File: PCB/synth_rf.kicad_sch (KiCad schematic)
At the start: 63 parts, among them J2 SMA CLK0, J3 SMA CLK1, J4 SMA CLK2, U2 Si5351A-B-GT, X1 25MHz TCXO

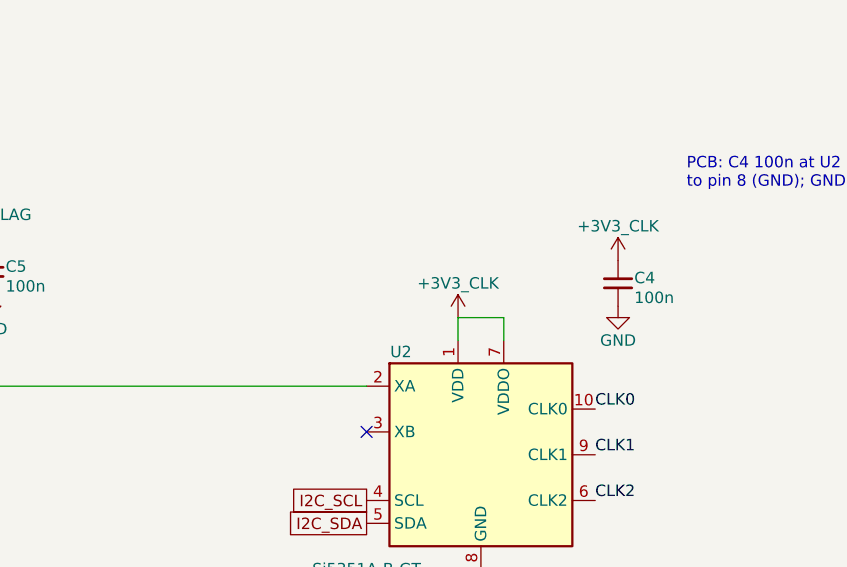
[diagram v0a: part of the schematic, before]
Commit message: U2 decoupling: C26 100n at VDDO (pin 7), C27 10u + C28 100n bulk on +3V3_CLK after FB1, caps inline at the U2 supply pins; RF50 netclass (0.31 mm) incl. CLK0-2_BYP lanes; regen docs
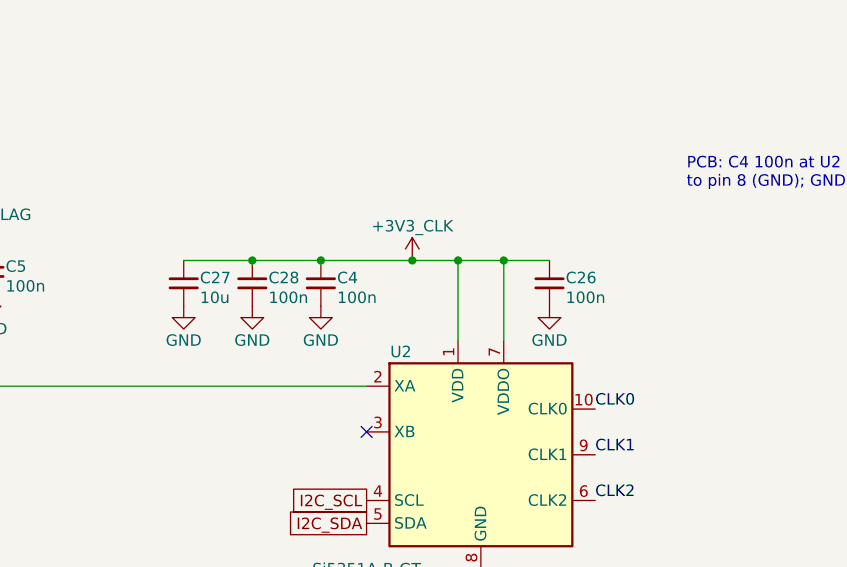
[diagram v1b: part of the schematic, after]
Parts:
- added C26, C28: 100n, Capacitor_SMD:C_0805_2012Metric, symbol Device:C_Small
- added C27: 10u, Capacitor_SMD:C_0805_2012Metric, symbol Device:C_Small
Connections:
- net +3V3_CLK: now also C26.1, C27.1, C28.1
- net GND: now also C26.2, C27.2, C28.2
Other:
- moved on the sheet: C4

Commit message: R100/R120/R140 -> 0402 0R (C17168) and C26 -> 0402 100n (C1525) so the series R and VDDO cap fit at U2's 0.5 mm-pitch CLK/VDDO pins; regen docs
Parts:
- C26: footprint Capacitor_SMD:C_0805_2012Metric -> Capacitor_SMD:C_0402_1005Metric; LCSC C49678 -> C1525; MPN CC0805KRX7R9BB104 -> CL05B104KO5NNNC; Manufacturer YAGEO -> Samsung Electro-Mechanics
- R100, R120, R140: footprint Resistor_SMD:R_0805_2012Metric -> Resistor_SMD:R_0402_1005Metric; LCSC C17477 -> C17168; MPN 0805W8F0000T5E -> 0402WGF0000TCE
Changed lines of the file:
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@@
 			)
 		)
-		(property "Footprint" "Resistor_SMD:R_0805_2012Metric"
+		(property "Footprint" "Resistor_SMD:R_0402_1005Metric"
 			(at 40.64 172.72 0)
 			(hide yes)
@@
 			)
 		)
-		(property "LCSC" "C17477"
+		(property "LCSC" "C17168"
 			(at 40.64 172.72 0)
 			(hide yes)
@@
 			)
 		)
-		(property "MPN" "0805W8F0000T5E"
+		(property "MPN" "0402WGF0000TCE"
 			(at 40.64 172.72 0)
 			(hide yes)
@@
 			)
 		)
-		(property "Footprint" "Resistor_SMD:R_0805_2012Metric"
+		(property "Footprint" "Resistor_SMD:R_0402_1005Metric"
 			(at 40.64 264.16 0)
 			(hide yes)
@@
 			)
 		)
-		(property "LCSC" "C17477"
+		(property "LCSC" "C17168"
 			(at 40.64 264.16 0)
 			(hide yes)
@@
 			)
 		)
-		(property "MPN" "0805W8F0000T5E"
+		(property "MPN" "0402WGF0000TCE"
 			(at 40.64 264.16 0)
 			(hide yes)
@@
 			)
 		)
-		(property "Footprint" "Resistor_SMD:R_0805_2012Metric"
+		(property "Footprint" "Resistor_SMD:R_0402_1005Metric"
 			(at 40.64 218.44 0)
 			(hide yes)
@@
 			)
 		)
-		(property "LCSC" "C17477"
+		(property "LCSC" "C17168"
 			(at 40.64 218.44 0)
 			(hide yes)
@@
 			)
 		)
-		(property "MPN" "0805W8F0000T5E"
+		(property "MPN" "0402WGF0000TCE"
 			(at 40.64 218.44 0)
 			(hide yes)
@@
 			)
 		)
-		(property "Footprint" "Capacitor_SMD:C_0805_2012Metric"
+		(property "Footprint" "Capacitor_SMD:C_0402_1005Metric"
 			(at 147.32 76.2 0)
 			(hide yes)
@@
 			)
 		)
-		(property "LCSC" "C49678"
+		(property "LCSC" "C1525"
 			(at 147.32 76.2 0)
 			(hide yes)
@@
 			)
 		)
-		(property "MPN" "CC0805KRX7R9BB104"
+		(property "MPN" "CL05B104KO5NNNC"
 			(at 147.32 76.2 0)
 			(hide yes)
@@
 			)
 		)
-		(property "Manufacturer" "YAGEO"
+		(property "Manufacturer" "Samsung Electro-Mechanics"
 			(at 147.32 76.2 0)
 			(hide yes)
